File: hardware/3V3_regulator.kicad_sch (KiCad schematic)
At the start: 5 parts, among them U4 AP2111H-3.3

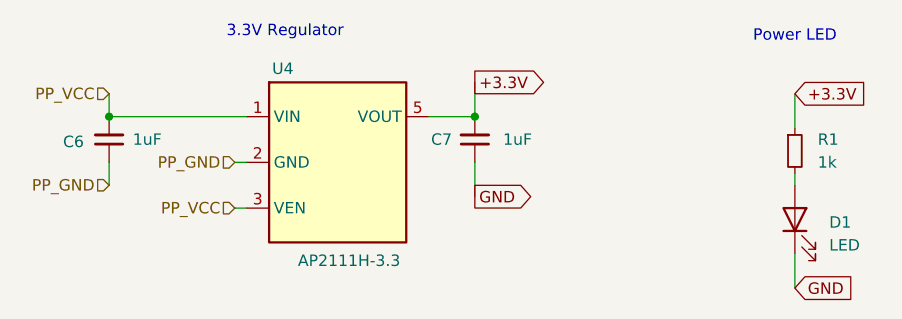
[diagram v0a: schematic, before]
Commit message: Made the global labels for power visible in the main shchematic
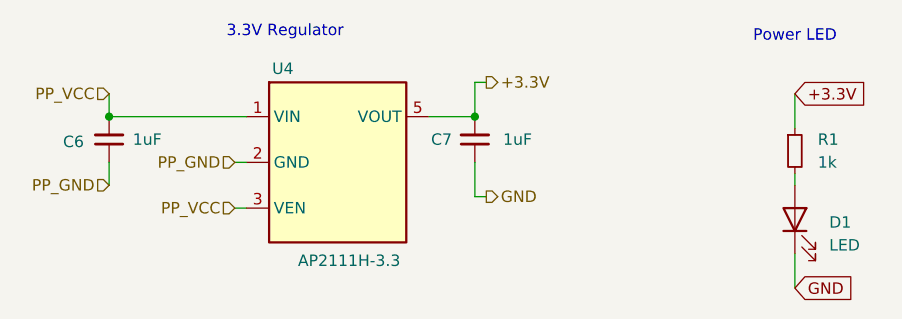
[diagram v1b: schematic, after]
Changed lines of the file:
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@@
-	(wire
-		(pts
-			(xy 133.35 69.85) (xy 133.35 73.66)
-		)
-		(stroke
-			(width 0)
-			(type default)
-		)
-	)
 	(wire
 		(pts
@@
 	(wire
 		(pts
+			(xy 133.35 82.55) (xy 133.35 78.74)
+		)
+		(stroke
+			(width 0)
+			(type default)
+		)
+	)
+	(wire
+		(pts
 			(xy 92.71 71.12) (xy 92.71 73.66)
+		)
+		(stroke
+			(width 0)
+			(type default)
+		)
+	)
+	(wire
+		(pts
+			(xy 134.62 82.55) (xy 133.35 82.55)
 		)
 		(stroke
@@
 	(wire
 		(pts
+			(xy 134.62 69.85) (xy 133.35 69.85)
+		)
+		(stroke
+			(width 0)
+			(type default)
+		)
+	)
+	(wire
+		(pts
 			(xy 107.95 73.66) (xy 92.71 73.66)
 		)
@@
 	(wire
 		(pts
-			(xy 133.35 78.74) (xy 133.35 82.55)
+			(xy 133.35 69.85) (xy 133.35 73.66)
 		)
 		(stroke
@@
 		)
 	)
-	(global_label "GND"
-		(shape output)
-		(at 133.35 82.55 0)
-		(fields_autoplaced yes)
-		(effects
-			(font
-				(size 1.27 1.27)
-			)
-			(justify left)
-		)
-		(property "Intersheetrefs" "${INTERSHEET_REFS}"
-			(at 140.2057 82.55 0)
-			(effects
-				(font
-					(size 1.27 1.27)
-				)
-				(justify left)
-				(hide yes)
-			)
-		)
-	)
-	(global_label "+3.3V"
-		(shape output)
-		(at 133.35 69.85 0)
-		(fields_autoplaced yes)
-		(effects
-			(font
-				(size 1.27 1.27)
-			)
-			(justify left)
-		)
-		(property "Intersheetrefs" "${INTERSHEET_REFS}"
-			(at 142.02 69.85 0)
-			(effects
-				(font
-					(size 1.27 1.27)
-				)
-				(justify left)
-				(hide yes)
-			)
-		)
-	)
 	(hierarchical_label "PP_GND"
 		(shape input)
@@
 			)
 			(justify right)
+		)
+	)
+	(hierarchical_label "GND"
+		(shape output)
+		(at 134.62 82.55 0)
+		(fields_autoplaced yes)
+		(effects
+			(font
+				(size 1.27 1.27)
+			)
+			(justify left)
 		)
 	)
@@
 		)
 	)
+	(hierarchical_label "+3.3V"
+		(shape output)
+		(at 134.62 69.85 0)
+		(fields_autoplaced yes)
+		(effects
+			(font
+				(size 1.27 1.27)
+			)
+			(justify left)
+		)
+	)

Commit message: Added information, footprints and 3d models for several components
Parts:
- U4: footprint (none) -> Package_TO_SOT_SMD:SOT-223; Package (none) -> SOT-223; Part Num (none) -> AP2111H-3.3TRG1; Price/unit (none) -> $0.1080; Supplier Link (none) -> https://jlcpcb.com/partdetail/DiodesIncorporated-AP2111H_33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
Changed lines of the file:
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@@
 			)
 		)
-		(property "Footprint" ""
+		(property "Footprint" "Package_TO_SOT_SMD:SOT-223"
 			(at 115.57 77.47 0)
 			(effects
@@
 			)
 		)
-		(property "Datasheet" ""
+		(property "Datasheet" "https://jlcpcb.com/api/file/downloadByFileSystemAccessId/8560080384345341952"
 			(at 115.57 77.47 0)
 			(effects
@@
 			)
 		)
-		(property "Description" ""
+		(property "Description" "65dB@(100Hz,1kHz) 600mA Fixed 3.3V Positive electrode 6V SOT-223 Voltage Regulators - Linear, Low Drop Out (LDO) Regulators ROHS"
 			(at 115.57 77.47 0)
 			(effects
 				(font
+					(size 1.27 1.27)
+				)
+				(hide yes)
+			)
+		)
+		(property "Supplier Link" "https://jlcpcb.com/partdetail/DiodesIncorporated-AP2111H_33TRG1/C155300"
+			(at 118.11 78.74 0)
+			(effects
+				(font
+					(size 1.27 1.27)
+				)
+				(hide yes)
+			)
+		)
+		(property "Price/unit" " $0.1080"
+			(at 118.11 78.74 0)
+			(effects
+				(font
+					(size 1.27 1.27)
+				)
+				(hide yes)
+			)
+		)
+		(property "Part Num" " AP2111H-3.3TRG1"
+			(at 118.11 78.74 0)
+			(effects
+				(font
+					(size 1.27 1.27)
+				)
+				(hide yes)
+			)
+		)
+		(property "Package" "SOT-223"
+			(at 118.11 78.74 0)
+			(effects
+				(font
